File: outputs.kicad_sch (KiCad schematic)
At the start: 25 parts, among them U10 ULN2004, U9 ULN2004

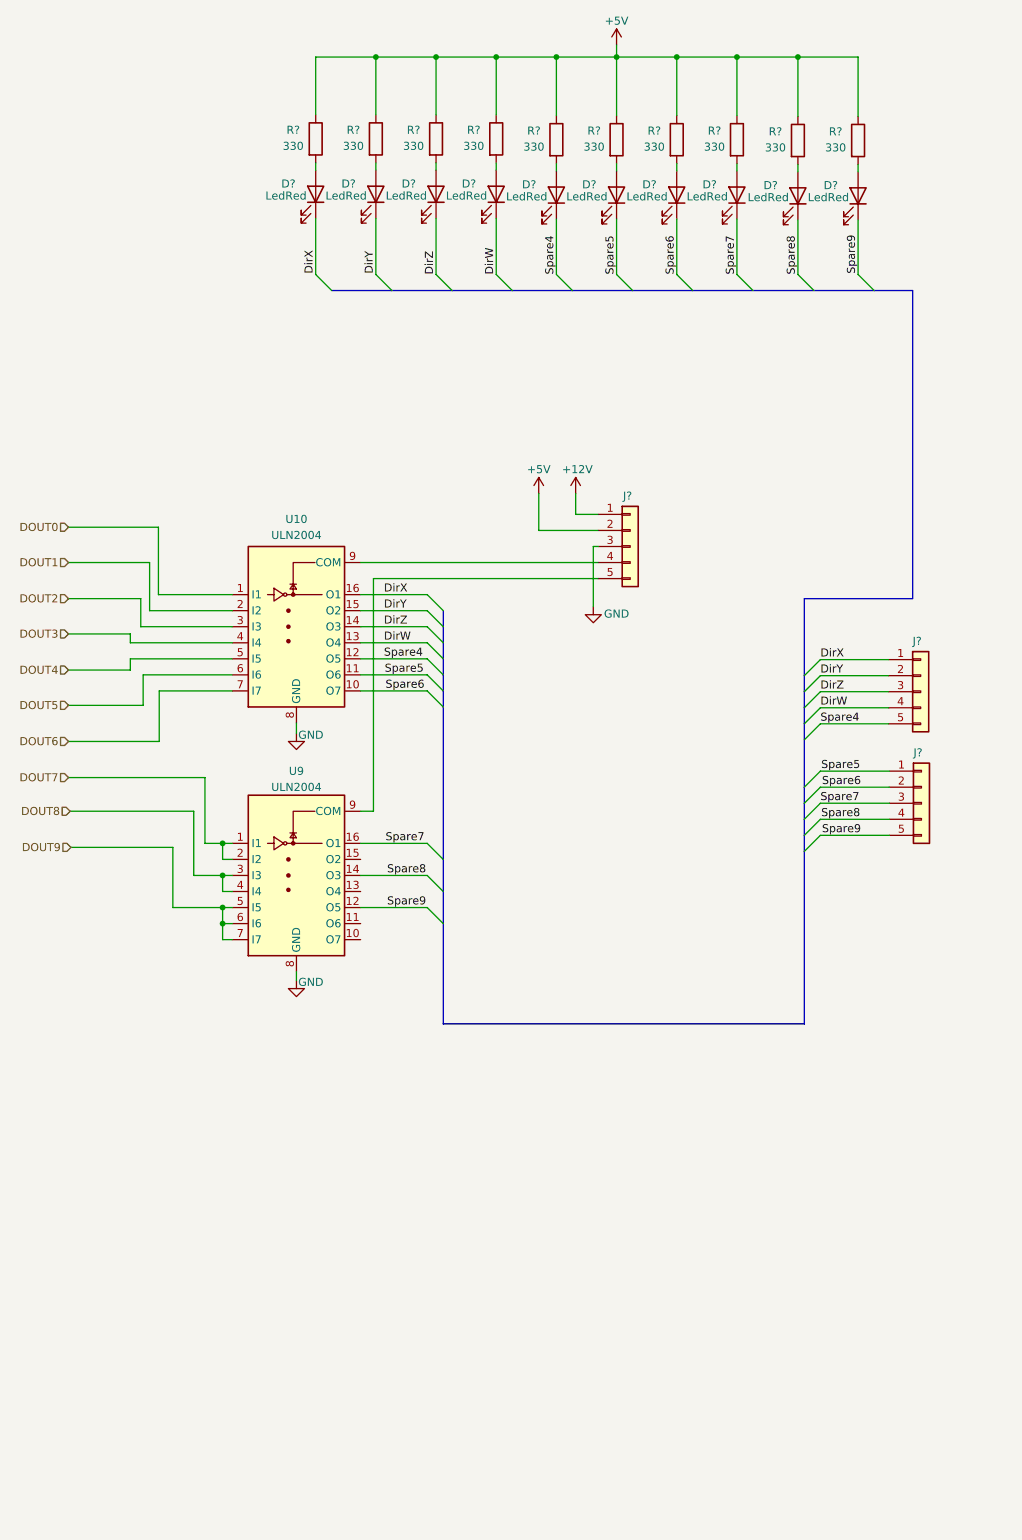
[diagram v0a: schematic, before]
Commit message: Avances en corrección de errores en conexiones eléctricas (ERC).
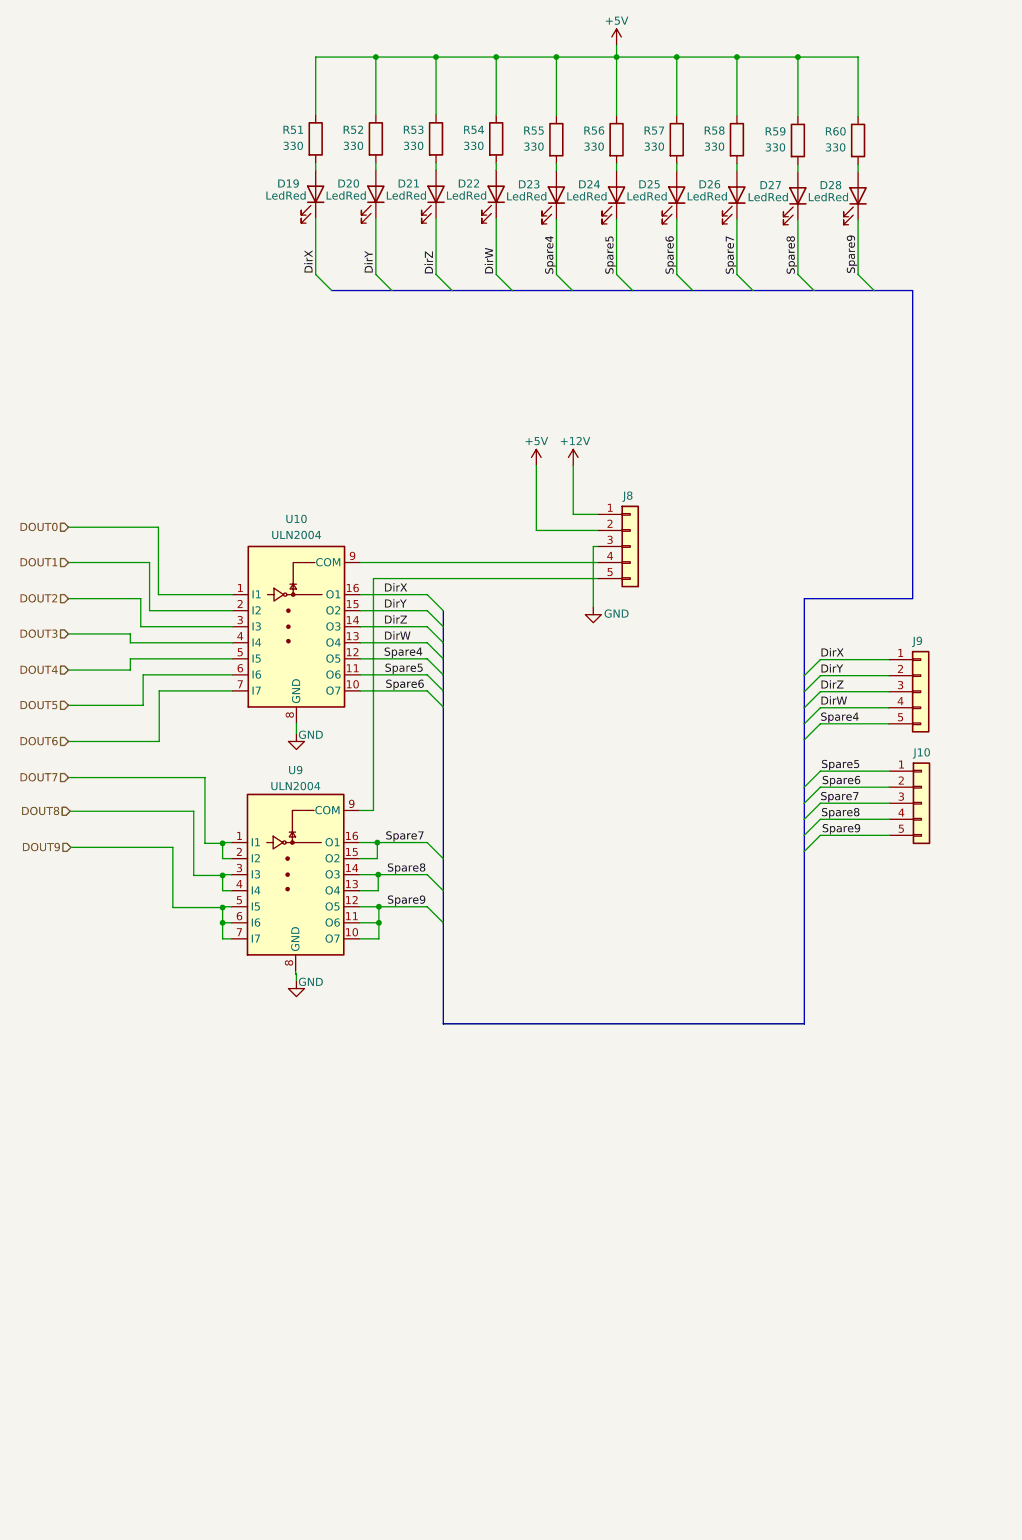
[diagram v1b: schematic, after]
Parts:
- gave numbers to parts that had none: 23
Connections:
- net Spare7: now also U9.15 (O2)
- net Spare8: now also U9.13 (O4)
- net Spare9: now also U9.10 (O7), U9.11 (O6)

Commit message: Se corrigieron errores de conexión. Falta asignar footprints aún
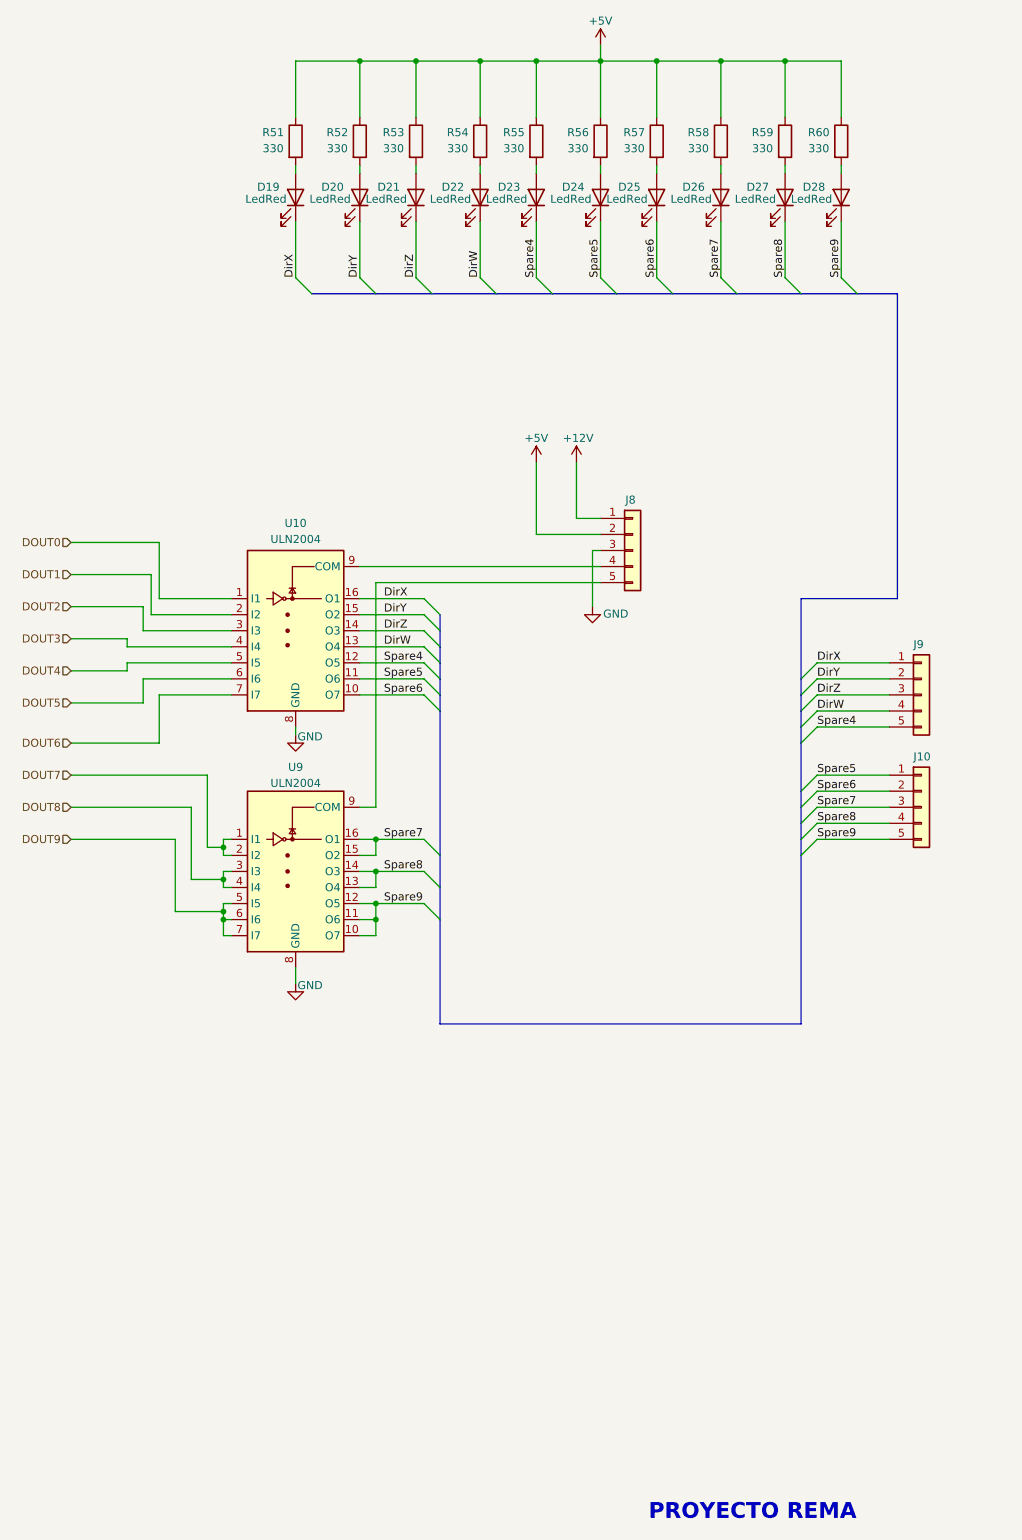
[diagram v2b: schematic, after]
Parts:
- D19, D20, D21, D22, D23, D24, D25, D26, D27, D28: footprint (none) -> LED_SMD:LED_1206_3216Metric
- R51, R52, R53, R54, R55, R56, R57, R58, R59, R60: footprint (none) -> Resistor_SMD:R_1206_3216Metric
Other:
- note added: "PROYECTO REMA"
- title: (none) -> Salidas
- moved on the sheet: D19, D20, D21, D22, D23, D24, D25, D26, D27, D28, J10, J8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

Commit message: Esquemático listo, sin errores de conexión y con todos los footprints especificados
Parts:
- J10, J8, J9: footprint (none) -> Connector_PinHeader_2.54mm:PinHeader_1x05_P2.54mm_Vertical
- U10, U9: footprint (none) -> Package_SO:SO-16_3.9x9.9mm_P1.27mm
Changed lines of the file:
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@@
 			)
 		)
-		(property "Footprint" ""
+		(property "Footprint" "Package_SO:SO-16_3.9x9.9mm_P1.27mm"
 			(at 69.85 135.89 0)
 			(effects
@@
 			)
 		)
-		(property "Footprint" ""
+		(property "Footprint" "Connector_PinHeader_2.54mm:PinHeader_1x05_P2.54mm_Vertical"
 			(at 121.92 109.22 0)
 			(effects
@@
 			)
 		)
-		(property "Footprint" ""
+		(property "Footprint" "Connector_PinHeader_2.54mm:PinHeader_1x05_P2.54mm_Vertical"
 			(at 167.64 132.08 0)
 			(effects
@@
 			)
 		)
-		(property "Footprint" ""
+		(property "Footprint" "Connector_PinHeader_2.54mm:PinHeader_1x05_P2.54mm_Vertical"
 			(at 167.64 149.86 0)
 			(effects
@@
 			)
 		)
-		(property "Footprint" ""
+		(property "Footprint" "Package_SO:SO-16_3.9x9.9mm_P1.27mm"
 			(at 69.85 173.99 0)
 			(effects

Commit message: Comienza el diseño del pcb
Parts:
- added TP12, TP5: TestPoint, TestPoint:TestPoint_Pad_D2.0mm, symbol Connector:TestPoint
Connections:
- net +12V: now also TP12.1
- net +5V: now also TP5.1
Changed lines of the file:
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@@
 	)
 	(junction
+		(at 113.03 97.79)
+		(diameter 0)
+		(color 0 0 0 0)
+	)
+	(junction
 		(at 135.89 31.75)
 		(diameter 0)
@@
 	)
 	(junction
+		(at 106.68 97.79)
+		(diameter 0)
+		(color 0 0 0 0)
+	)
+	(junction
 		(at 125.73 31.75)
 		(diameter 0)
@@
 	(wire
 		(pts
+			(xy 119.38 96.52) (xy 119.38 97.79)
+		)
+		(stroke
+			(width 0)
+			(type default)
+		)
+	)
+	(wire
+		(pts
 			(xy 146.05 57.15) (xy 146.05 66.04)
 		)
@@
 	(wire
 		(pts
+			(xy 100.33 97.79) (xy 106.68 97.79)
+		)
+		(stroke
+			(width 0)
+			(type default)
+		)
+	)
+	(wire
+		(pts
 			(xy 44.45 133.35) (xy 44.45 129.54)
 		)
@@
 	(wire
 		(pts
+			(xy 119.38 97.79) (xy 113.03 97.79)
+		)
+		(stroke
+			(width 0)
+			(type default)
+		)
+	)
+	(wire
+		(pts
 			(xy 151.13 144.78) (xy 162.56 144.78)
 		)
@@
 	(wire
 		(pts
+			(xy 100.33 96.52) (xy 100.33 97.79)
+		)
+		(stroke
+			(width 0)
+			(type default)
+		)
+	)
+	(wire
+		(pts
 			(xy 54.61 156.21) (xy 57.15 156.21)
 		)
@@
 	(wire
 		(pts
+			(xy 106.68 97.79) (xy 106.68 106.68)
+		)
+		(stroke
+			(width 0)
+			(type default)
+		)
+	)
+	(wire
+		(pts
 			(xy 151.13 149.86) (xy 162.56 149.86)
 		)
@@
 	(wire
 		(pts
+			(xy 113.03 97.79) (xy 113.03 95.25)
+		)
+		(stroke
+			(width 0)
+			(type default)
+		)
+	)
+	(wire
+		(pts
 			(xy 135.89 40.64) (xy 135.89 31.75)
 		)
@@
 		)
 	)
+	(wire
+		(pts
+			(xy 106.68 95.25) (xy 106.68 97.79)
+		)
+		(stroke
+			(width 0)
+			(type default)
+		)
+	)
 	(bus
 		(pts
@@
 	(wire
 		(pts
-			(xy 106.68 95.25) (xy 106.68 106.68)
-		)
-		(stroke
-			(width 0)
-			(type default)
-		)
-	)
-	(wire
-		(pts
 			(xy 97.79 48.26) (xy 97.79 49.53)
 		)
@@
 	(wire
 		(pts
+			(xy 113.03 97.79) (xy 113.03 104.14)
+		)
+		(stroke
+			(width 0)
+			(type default)
+		)
+	)
+	(wire
+		(pts
 			(xy 68.58 48.26) (xy 68.58 49.53)
 		)
@@
 	(wire
 		(pts
-			(xy 113.03 95.25) (xy 113.03 104.14)
-		)
-		(stroke
-			(width 0)
-			(type default)
-		)
-	)
-	(wire
-		(pts
 			(xy 78.74 157.48) (xy 81.28 157.48)
 		)
@@
 	)
 	(symbol
+		(lib_id "Connector:TestPoint")
+		(at 100.33 96.52 0)
+		(unit 1)
+		(exclude_from_sim yes)
+		(in_bom yes)
+		(on_board yes)
+		(dnp no)
+		(property "Reference" "TP5"
+			(at 96.52 91.44 0)
+			(effects
+				(font
+					(size 1.27 1.27)
+				)
+				(justify left)
+			)
+		)
+		(property "Value" "TestPoint"
+			(at 90.17 95.25 0)
+			(effects
+				(font
+					(size 1.27 1.27)
+				)
+				(justify left)
+				(hide yes)
+			)
+		)
+		(property "Footprint" "TestPoint:TestPoint_Pad_D2.0mm"
+			(at 105.41 96.52 0)
+			(effects
+				(font
+					(size 1.27 1.27)
+				)
+				(hide yes)
+			)
+		)
+		(property "Datasheet" "~"
+			(at 105.41 96.52 0)
+			(effects
+				(font
+					(size 1.27 1.27)
+				)
+				(hide yes)
+			)
+		)
+		(property "Description" "test point"
+			(at 100.33 96.52 0)
+			(effects
+				(font
+					(size 1.27 1.27)
+				)
+				(hide yes)
+			)
+		)
+		(pin "1"
+		)
+		(instances
+			(project "PonchoRema"
+				(path "/5eaa4ad0-b04c-4c59-839d-734ec887be48/c94ce8ba-2702-4b75-b25a-edf52a8cbe5c"
+					(reference "TP5")
+					(unit 1)
+				)
+			)
+		)
+	)
+	(symbol
 		(lib_id "Device:R")
 		(at 78.74 44.45 0)
@@
 					(unit 1)
 				)
+			)
+		)
+	)
+	(symbol
+		(lib_id "Connector:TestPoint")
+		(at 119.38 96.52 0)
+		(unit 1)
+		(exclude_from_sim yes)
+		(in_bom yes)
+		(on_board yes)
+		(dnp no)
+		(property "Reference" "TP12"
+			(at 119.38 91.44 0)
+			(effects
+				(font
+					(size 1.27 1.27)
+				)
+				(justify left)
+			)
+		)
+		(property "Value" "TestPoint"
+			(at 121.92 94.4879 0)
+			(effects
+				(font
+					(size 1.27 1.27)
+				)
+				(justify left)
+				(hide yes)
+			)
+		)
+		(property "Footprint" "TestPoint:TestPoint_Pad_D2.0mm"
+			(at 124.46 96.52 0)
+			(effects
+				(font
+					(size 1.27 1.27)
+				)
+				(hide yes)
+			)
+		)
+		(property "Datasheet" "~"
+			(at 124.46 96.52 0)
+			(effects
+				(font
+					(size 1.27 1.27)
+				)
+				(hide yes)
+			)
+		)
+		(property "Description" "test point"
+			(at 119.38 96.52 0)
+			(effects
+				(font
+					(size 1.27 1.27)
+				)
+				(hide yes)
+			)
+		)
+		(pin "1"
+		)
+		(instances
+			(project "PonchoRema"
+				(path "/5eaa4ad0-b04c-4c59-839d-734ec887be48/c94ce8ba-2702-4b75-b25a-edf52a8cbe5c"
+					(reference "TP12")
+					(unit 1)
+				)

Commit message: Comienza ruteo en pcb
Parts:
- J10: value Conn_01x05 -> DOUT_5-9
- J9: value Conn_01x05 -> DOUT_0-4
- renumbered D19 to D20, D20 to D21, D21 to D22, D22 to D23, D23 to D24, D24 to D25, D25 to D26, D26 to D27, D27 to D28, D28 to D29
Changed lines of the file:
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@@
 		(on_board yes)
 		(dnp no)
-		(property "Reference" "D23"
+		(property "Reference" "D24"
 			(at 102.362 51.689 90)
 			(effects
@@
 					(size 1.27 1.27)
 				)
+				(hide yes)
 			)
 		)
@@
 			(project "PonchoRema"
 				(path "/5eaa4ad0-b04c-4c59-839d-734ec887be48/c94ce8ba-2702-4b75-b25a-edf52a8cbe5c"
-					(reference "D23")
+					(reference "D24")
 					(unit 1)
 				)
@@
 		(on_board yes)
 		(dnp no)
-		(property "Reference" "D27"
+		(property "Reference" "D28"
 			(at 141.732 51.689 90)
 			(effects
@@
 					(size 1.27 1.27)
 				)
+				(hide yes)
 			)
 		)
@@
 			(project "PonchoRema"
 				(path "/5eaa4ad0-b04c-4c59-839d-734ec887be48/c94ce8ba-2702-4b75-b25a-edf52a8cbe5c"
-					(reference "D27")
+					(reference "D28")
 					(unit 1)
 				)
@@
 		(on_board yes)
 		(dnp no)
-		(property "Reference" "D21"
+		(property "Reference" "D22"
 			(at 83.312 51.689 90)
 			(effects
@@
 					(size 1.27 1.27)
 				)
+				(hide yes)
 			)
 		)
@@
 			(project "PonchoRema"
 				(path "/5eaa4ad0-b04c-4c59-839d-734ec887be48/c94ce8ba-2702-4b75-b25a-edf52a8cbe5c"
-					(reference "D21")
+					(reference "D22")
 					(unit 1)
 				)
@@
 		(on_board yes)
 		(dnp no)
-		(property "Reference" "D22"
+		(property "Reference" "D23"
 			(at 93.472 51.689 90)
 			(effects
@@
 					(size 1.27 1.27)
 				)
+				(hide yes)
 			)
 		)
@@
 			(project "PonchoRema"
 				(path "/5eaa4ad0-b04c-4c59-839d-734ec887be48/c94ce8ba-2702-4b75-b25a-edf52a8cbe5c"
-					(reference "D22")
+					(reference "D23")
 					(unit 1)
 				)
@@
 			)
 		)
-		(property "Value" "Conn_01x05"
-			(at 161.671 123.571 0)
+		(property "Value" "DOUT_0-4"
+			(at 170.18 132.08 0)
 			(effects
 				(font
@@
 				)
 				(justify left)
-				(hide yes)
 			)
 		)
@@
 			)
 		)
-		(property "Value" "Conn_01x05"
-			(at 161.671 141.351 0)
+		(property "Value" "DOUT_5-9"
+			(at 170.18 148.59 0)
 			(effects
 				(font
@@
 				)
 				(justify left)
-				(hide yes)
 			)
 		)
@@
 		(on_board yes)
 		(dnp no)
-		(property "Reference" "D19"
+		(property "Reference" "D20"
 			(at 64.262 51.689 90)
 			(effects
@@
 					(size 1.27 1.27)
 				)
+				(hide yes)
 			)
 		)
@@
 			(project "PonchoRema"
 				(path "/5eaa4ad0-b04c-4c59-839d-734ec887be48/c94ce8ba-2702-4b75-b25a-edf52a8cbe5c"
-					(reference "D19")
+					(reference "D20")
 					(unit 1)
 				)
@@
 		(on_board yes)
 		(dnp no)
-		(property "Reference" "D24"
+		(property "Reference" "D25"
 			(at 112.522 51.689 90)
 			(effects
@@
 					(size 1.27 1.27)
 				)
+				(hide yes)
 			)
 		)
@@
 			(project "PonchoRema"
 				(path "/5eaa4ad0-b04c-4c59-839d-734ec887be48/c94ce8ba-2702-4b75-b25a-edf52a8cbe5c"
-					(reference "D24")
+					(reference "D25")
 					(unit 1)
 				)
@@
 		(on_board yes)
 		(dnp no)
-		(property "Reference" "D25"
+		(property "Reference" "D26"
 			(at 121.412 51.689 90)
 			(effects
@@
 					(size 1.27 1.27)
 				)
+				(hide yes)
 			)
 		)
@@
 			(project "PonchoRema"
 				(path "/5eaa4ad0-b04c-4c59-839d-734ec887be48/c94ce8ba-2702-4b75-b25a-edf52a8cbe5c"
-					(reference "D25")
+					(reference "D26")
 					(unit 1)
 				)
@@
 		(on_board yes)
 		(dnp no)
-		(property "Reference" "D28"
+		(property "Reference" "D29"
 			(at 150.622 51.689 90)
 			(effects
@@
 					(size 1.27 1.27)
 				)
+				(hide yes)
 			)
 		)
@@
 			(project "PonchoRema"
 				(path "/5eaa4ad0-b04c-4c59-839d-734ec887be48/c94ce8ba-2702-4b75-b25a-edf52a8cbe5c"
-					(reference "D28")
+					(reference "D29")
 					(unit 1)
 				)
@@
 		(on_board yes)
 		(dnp no)
-		(property "Reference" "D20"
+		(property "Reference" "D21"
 			(at 74.422 51.689 90)
 			(effects
@@
 					(size 1.27 1.27)
 				)
+				(hide yes)
 			)
 		)
@@
 			(project "PonchoRema"
 				(path "/5eaa4ad0-b04c-4c59-839d-734ec887be48/c94ce8ba-2702-4b75-b25a-edf52a8cbe5c"
-					(reference "D20")
+					(reference "D21")
 					(unit 1)
 				)
@@
 		(on_board yes)
 		(dnp no)
-		(property "Reference" "D26"
+		(property "Reference" "D27"
 			(at 131.572 51.689 90)
 			(effects
@@
 					(size 1.27 1.27)
 				)
+				(hide yes)
 			)
 		)
@@
 			(project "PonchoRema"
 				(path "/5eaa4ad0-b04c-4c59-839d-734ec887be48/c94ce8ba-2702-4b75-b25a-edf52a8cbe5c"
-					(reference "D26")
-					(unit 1)
-				)
+					(reference "D27")
+					(unit 1)
+				)
